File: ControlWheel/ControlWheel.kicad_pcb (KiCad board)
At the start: 2 copper layers, 45.7 x 45.7 mm, 1 part, among them U1 AI12

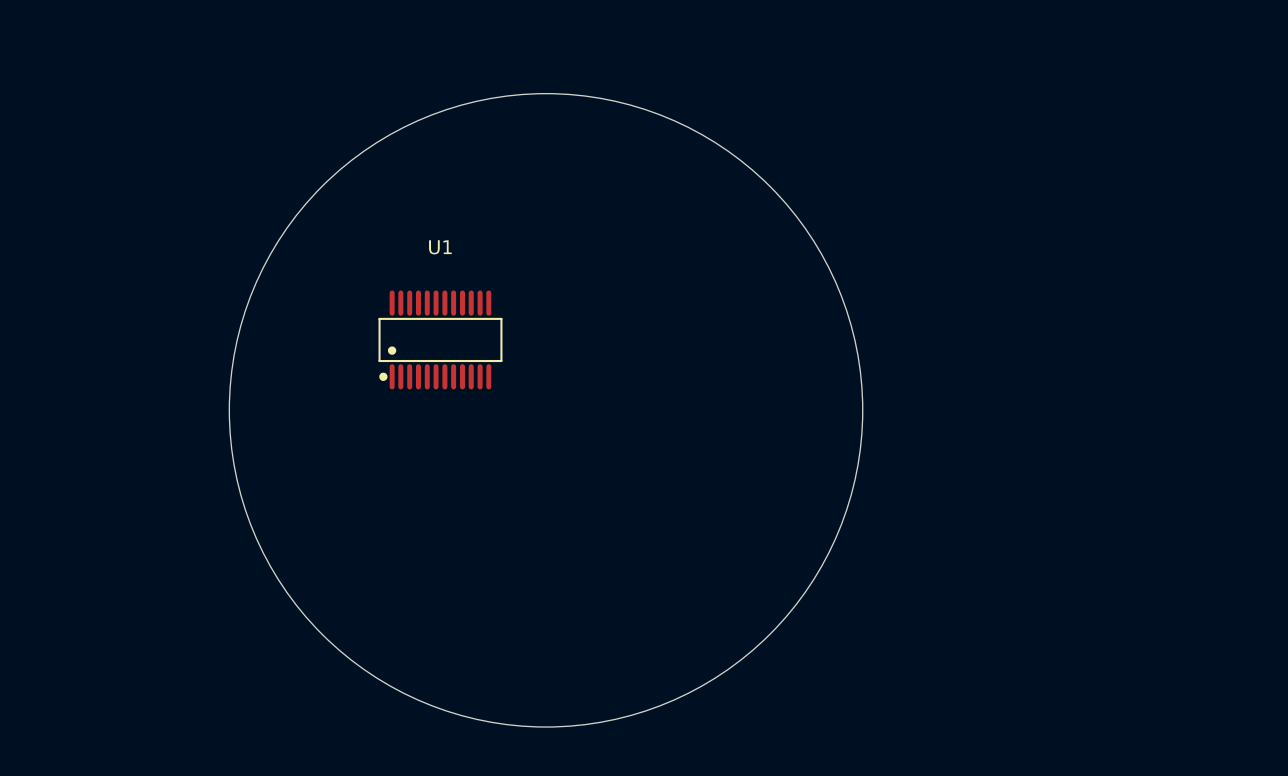
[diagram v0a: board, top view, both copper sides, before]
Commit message: footprints for wheel + power changes for v3s
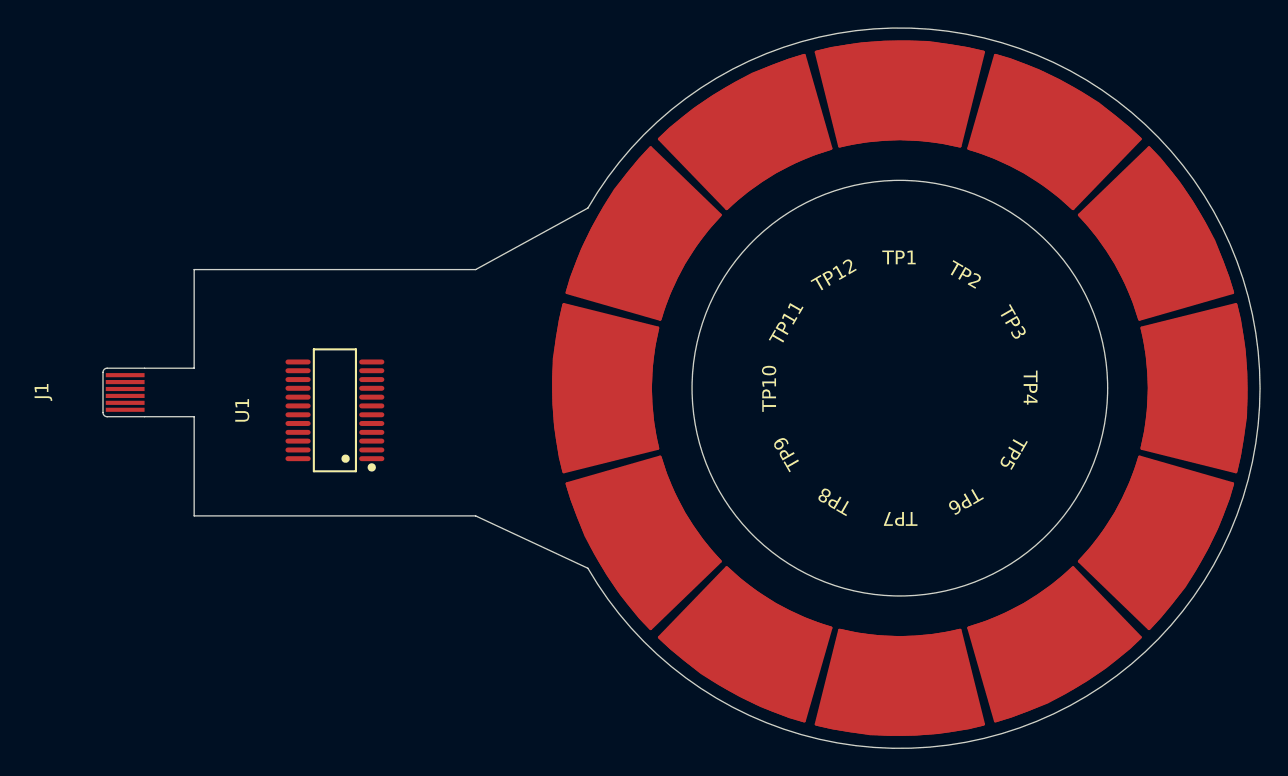
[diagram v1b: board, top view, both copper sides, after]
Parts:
- added J1: Conn_01x06_Pin, FlexPCB_FPC:6pin_0.5mm-Pitch, F.Cu at (92.5, 100.3)
- added TP1, TP10, TP11, TP12, TP2, TP3, TP4, TP5, TP6, TP7, TP8, TP9: TestPoint, CapTouchPads:RoundPad, F.Cu at (150.0, 100.0)
- moved U1 9.16 mm to (109.2, 101.6), turned to 90 degrees
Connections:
- U1 pad 1: unconnected-(U1-KEY1-Pad1) -> Net-(U1-KEY1)
- U1 pad 10: unconnected-(U1-KEY10-Pad10) -> Net-(U1-KEY10)
- U1 pad 11: unconnected-(U1-KEY11-Pad11) -> Net-(U1-KEY11)
- U1 pad 12: unconnected-(U1-KEY12-Pad12) -> Net-(U1-KEY12)
- U1 pad 13: unconnected-(U1-BCD3-Pad13) -> /BCD3
- U1 pad 14: unconnected-(U1-BCD2-Pad14) -> /BCD2
- U1 pad 15: unconnected-(U1-BCD1-Pad15) -> /BCD1
- U1 pad 16: unconnected-(U1-BCD0-Pad16) -> /BCD0
- U1 pad 17: unconnected-(U1-S2-Pad17) -> Net-(U1-S2-Pad17)
- U1 pad 18: unconnected-(U1-S2-Pad18) -> Net-(U1-S2-Pad17)
- U1 pad 19: unconnected-(U1-VDD-Pad19) -> +3.3V
- U1 pad 2: unconnected-(U1-KEY2-Pad2) -> Net-(U1-KEY2)
- U1 pad 21: unconnected-(U1-GND-Pad21) -> GND
- U1 pad 22: unconnected-(U1-C1-Pad22) -> Net-(U1-C1)
- U1 pad 23: unconnected-(U1-CG-Pad23) -> Net-(U1-CG)
- U1 pad 24: unconnected-(U1-CSEL-Pad24) -> Net-(U1-CSEL)
- U1 pad 3: unconnected-(U1-KEY3-Pad3) -> Net-(U1-KEY3)
- U1 pad 4: unconnected-(U1-KEY4-Pad4) -> Net-(U1-KEY4)
- U1 pad 5: unconnected-(U1-KEY5-Pad5) -> Net-(U1-KEY5)
- U1 pad 6: unconnected-(U1-KEY6-Pad6) -> Net-(U1-KEY6)
- U1 pad 7: unconnected-(U1-KEY7-Pad7) -> Net-(U1-KEY7)
- U1 pad 8: unconnected-(U1-KEY8-Pad8) -> Net-(U1-KEY8)
- U1 pad 9: unconnected-(U1-KEY9-Pad9) -> Net-(U1-KEY9)
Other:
- board size 45.7 x 45.7 mm -> 80.5 x 52 mm

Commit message: minor power changes
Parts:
- moved U1 5.12 mm to (114.3, 102.2)
- moved J1 5.12 mm to (97.6, 100.9)
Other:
- board size 80.5 x 52 mm -> 68.9 x 39 mm
